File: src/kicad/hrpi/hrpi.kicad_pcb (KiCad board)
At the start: 2 copper layers, 97.5 x 72.5 mm, 26 parts, among them P1 CONN_02X20, P10 CONN_01X01, P11 CONN_01X04, P12 CONN_01X05, P13 CONN_01X05, P14 CONN_01X05, P15 CONN_01X04, P16 CONN_01X04, P17 CONN_01X02, P2 CONN_02X04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

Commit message: BUGFIX
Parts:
- added D5: LED, LEDs:LED-3MM, F.Cu at (183.2, 141.8)
- added R7: R, Resistors_SMD:R_0805_HandSoldering, B.Cu at (188.6, 140.0)
- R1, R2: value 7k -> 10k
- R3, R4, R5: value R -> 470
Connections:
- U2 pad 10: (no net) -> /RCOK
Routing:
- net /RCOK: track 0.00 -> 35.6 mm, vias 0 -> 2
- net Net-(D5-Pad1): track 0.00 -> 5.67 mm
- net /GND: track 222.8 -> 225.8 mm
- net /SDA: track 110.1 -> 109.4 mm

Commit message: Replaced power jumper
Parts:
- removed P10: CONN_01X01, Pin_Headers:Pin_Header_Straight_1x01
- P9: value CONN_01X01 -> CONN_01X02; footprint Pin_Headers:Pin_Header_Straight_1x01 -> Pin_Headers:Pin_Header_Straight_1x02
- moved P9 31.3 mm to (179.4, 171.2)
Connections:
- P9 pad 1: /RAIL -> /5V
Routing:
- net /RAIL: track 93.0 -> 113.5 mm, vias 0 -> 2
- net /5V: track 174.0 -> 175.2 mm
- net /GND: track 225.8 -> 227.0 mm

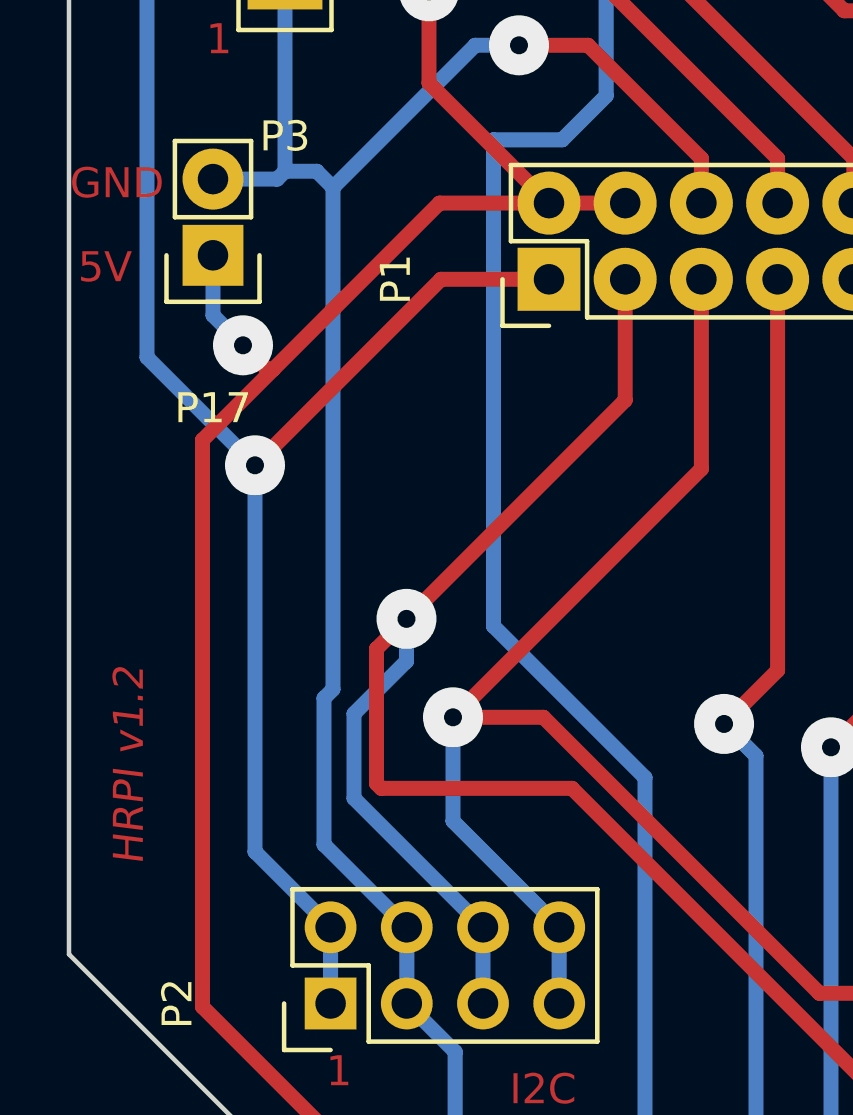
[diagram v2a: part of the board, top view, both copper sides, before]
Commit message: Some traces moved
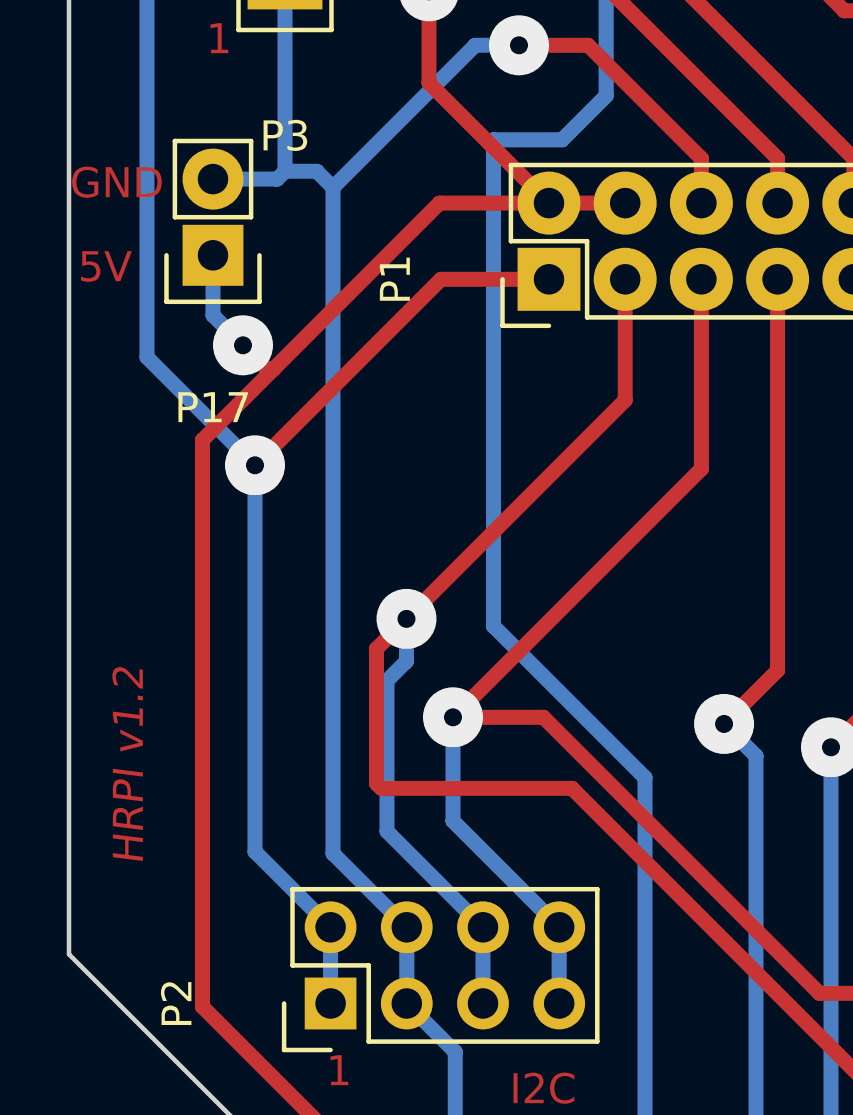
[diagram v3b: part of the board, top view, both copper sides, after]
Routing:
- net /SDA: track 109.4 -> 108.5 mm
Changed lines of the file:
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@@
     (links 107)
     (no_connects 0)
-    (area 129.924999 104.924999 227.575001 177.575001)
+    (area 129.391667 101.811666 229.375 177.575001)
     (thickness 1.6)
-    (drawings 55)
-    (tracks 512)
+    (drawings 57)
+    (tracks 510)
     (zones 0)
     (modules 27)
@@
     (pad_to_mask_clearance 0)
     (aux_axis_origin 143.5 181)
-    (visible_elements 7FFFFFFF)
+    (visible_elements 7FFFEFFF)
     (pcbplotparams
       (layerselection 0x00030_80000001)
@@
     )
   )
+  (target plus (at 136.8 167.2) (size 5) (width 0.15) (layer Edge.Cuts))
+  (target plus (at 219.4 123.8) (size 5) (width 0.15) (layer Edge.Cuts))
+  (target plus (at 224.4 153.4) (size 5) (width 0.15) (layer Edge.Cuts))
   (gr_text 1 (at 167.8 112.2) (layer F.Cu)
     (effects (font (size 1 1) (thickness 0.25)))
@@
     (effects (font (size 1 1) (thickness 0.25)))
   )
-  (target plus (at 183 171) (size 5) (width 0.15) (layer Edge.Cuts))
   (target plus (at 225 175) (size 5) (width 0.15) (layer Edge.Cuts))
   (target plus (at 132.5 107.5) (size 5) (width 0.15) (layer Edge.Cuts))
@@
   (via (at 136.2 136.2) (size 2) (drill 0.6) (layers F.Cu B.Cu) (net 3))
   (segment (start 138.72 151.6) (end 138.72 154.14) (width 0.5) (layer B.Cu) (net 3) (status 30))
+  (segment (start 138.8 126.94) (end 138.8 149.14) (width 0.5) (layer B.Cu) (net 4))
+  (segment (start 138.8 149.14) (end 141.26 151.6) (width 0.5) (layer B.Cu) (net 4))
   (segment (start 175.750001 167.440001) (end 174.090002 169.1) (width 0.5) (layer B.Cu) (net 4))
   (segment (start 175.750001 160.155257) (end 175.750001 167.440001) (width 0.5) (layer B.Cu) (net 4))
@@
   (segment (start 212.193601 137.970001) (end 211.9436 137.72) (width 0.5) (layer B.Cu) (net 4))
   (segment (start 211.9436 137.72) (end 210.58 137.72) (width 0.5) (layer B.Cu) (net 4) (status 20))
-  (segment (start 138.8 143.663948) (end 138.499968 143.96398) (width 0.5) (layer B.Cu) (net 4))
-  (segment (start 138.499968 148.839968) (end 141.26 151.6) (width 0.5) (layer B.Cu) (net 4) (status 20))
-  (segment (start 138.499968 143.96398) (end 138.499968 148.839968) (width 0.5) (layer B.Cu) (net 4))
-  (segment (start 138.8 126.94) (end 138.8 143.663948) (width 0.5) (layer B.Cu) (net 4))
   (segment (start 143.54 122.2) (end 145 122.2) (width 0.5) (layer B.Cu) (net 4))
   (segment (start 147.304924 122.2) (end 145 122.2) (width 0.5) (layer F.Cu) (net 4))
@@
   (via (at 142 120.4) (size 2) (drill 0.6) (layers F.Cu B.Cu) (net 5))
   (segment (start 187.643717 171.163717) (end 187.68 171.2) (width 0.5) (layer B.Cu) (net 5) (status 30))
+  (segment (start 143.8 151.6) (end 140.6 148.4) (width 0.5) (layer B.Cu) (net 6))
+  (segment (start 140.6 148.4) (end 140.6 143.383795) (width 0.5) (layer B.Cu) (net 6))
+  (segment (start 140.6 143.383795) (end 141.24998 142.733815) (width 0.5) (layer B.Cu) (net 6))
+  (segment (start 141.24998 142.733815) (end 141.24998 141.319602) (width 0.5) (layer B.Cu) (net 6))
   (segment (start 140.249981 142.319601) (end 141.24998 141.319602) (width 0.5) (layer F.Cu) (net 6))
   (segment (start 140.249981 146.808204) (end 140.249981 142.319601) (width 0.5) (layer F.Cu) (net 6))
@@
   (segment (start 140.409978 146.968201) (end 140.249981 146.808204) (width 0.5) (layer F.Cu) (net 6))
   (segment (start 200.2 158.2) (end 158 158.2) (width 0.5) (layer F.Cu) (net 6))
-  (segment (start 141.24998 142.733815) (end 141.24998 141.319602) (width 0.5) (layer B.Cu) (net 6))
   (via (at 141.24998 141.319602) (size 2) (drill 0.6) (layers F.Cu B.Cu) (net 6))
-  (segment (start 139.499979 144.483816) (end 141.24998 142.733815) (width 0.5) (layer B.Cu) (net 6))
   (segment (start 148.54 130) (end 148.54 134.029582) (width 0.5) (layer F.Cu) (net 6) (status 10))
   (segment (start 148.54 134.029582) (end 141.24998 141.319602) (width 0.5) (layer F.Cu) (net 6))
-  (segment (start 143.8 151.6) (end 139.499979 147.299979) (width 0.5) (layer B.Cu) (net 6) (status 10))
-  (segment (start 139.499979 147.299979) (end 139.499979 144.483816) (width 0.5) (layer B.Cu) (net 6))
   (segment (start 200.343717 149.051541) (end 200.343717 158.056283) (width 0.5) (layer B.Cu) (net 6) (status 10))
   (segment (start 200.343717 158.056283) (end 200.2 158.2) (width 0.5) (layer B.Cu) (net 6))
